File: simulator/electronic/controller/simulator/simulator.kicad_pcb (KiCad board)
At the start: 2 copper layers, 151 x 92.5 mm, 5 parts, among them J1 Mover1, J4 Mover2, J6 Rotator, J8 Mover3, U1 ESP32 D1 Mini

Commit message: design schematics
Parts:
- added D1: LED_PULSE, LED_SMD:LED_0805_2012Metric, B.Cu at (120.3, 75.2)
- added D10: LED_PULSE, LED_SMD:LED_0805_2012Metric, B.Cu at (49.5, 64.4)
- added D11: LED_DIR, LED_SMD:LED_RGB_5050-6, B.Cu at (47.6, 52.9)
- added D12: LED_SW, LED_SMD:LED_RGB_5050-6, B.Cu at (47.6, 59.6)
- added D2: LED_DIR, LED_SMD:LED_RGB_5050-6, B.Cu at (120.3, 80.1)
- added D3: LED_SW, LED_SMD:LED_RGB_5050-6, B.Cu at (120.3, 86.8)
- added D4: LED_PULSE, LED_SMD:LED_0805_2012Metric, B.Cu at (49.5, 84.1)
- added D5: LED_DIR, LED_SMD:LED_RGB_5050-6, B.Cu at (47.6, 72.6)
- added D6: LED_SW, LED_SMD:LED_RGB_5050-6, B.Cu at (47.6, 79.3)
- added D7: LED_PULSE, LED_SMD:LED_0805_2012Metric, B.Cu at (79.0, 64.4)
- added D8: LED_DIR, LED_SMD:LED_RGB_5050-6, B.Cu at (77.1, 52.9)
- added D9: LED_SW, LED_SMD:LED_RGB_5050-6, B.Cu at (77.1, 59.6)
- added J2: Conn_01x04_Socket, Connector_Extra:JST_XH_B4B-XH-A_1x04_P2.54mm_Vertical, F.Cu at (113.3, 91.4)
- added J3: Conn_01x04_Socket, Connector_Extra:JST_XH_B4B-XH-A_1x04_P2.54mm_Vertical, F.Cu at (113.3, 108.2)
- added J5: Conn_01x04_Socket, Connector_Extra:JST_XH_B4B-XH-A_1x04_P2.54mm_Vertical, F.Cu at (176.3, 84.8)
- added J7: Conn_01x04_Socket, Connector_Extra:JST_XH_B4B-XH-A_1x04_P2.54mm_Vertical, F.Cu at (176.3, 115.3)
- added R1: R_Small, Resistor_SMD:R_0805_2012Metric_Pad1.20x1.40mm_HandSolder, B.Cu at (127.0, 75.2)
- added R10: R_Small, Resistor_SMD:R_0805_2012Metric_Pad1.20x1.40mm_HandSolder, B.Cu at (68.6, 79.5)
- added R11: R_Small, Resistor_SMD:R_0805_2012Metric_Pad1.20x1.40mm_HandSolder, B.Cu at (68.6, 82.5)
- added R12: R_Small, Resistor_SMD:R_0805_2012Metric_Pad1.20x1.40mm_HandSolder, B.Cu at (68.6, 85.4)
- added R13: R_Small, Resistor_SMD:R_0805_2012Metric_Pad1.20x1.40mm_HandSolder, B.Cu at (98.1, 51.0)
- added R14: R_Small, Resistor_SMD:R_0805_2012Metric_Pad1.20x1.40mm_HandSolder, B.Cu at (98.1, 53.9)
- added R15: R_Small, Resistor_SMD:R_0805_2012Metric_Pad1.20x1.40mm_HandSolder, B.Cu at (98.1, 56.9)
- added R16: R_Small, Resistor_SMD:R_0805_2012Metric_Pad1.20x1.40mm_HandSolder, B.Cu at (98.1, 59.8)
- added R17: R_Small, Resistor_SMD:R_0805_2012Metric_Pad1.20x1.40mm_HandSolder, B.Cu at (98.1, 62.8)
- added R18: R_Small, Resistor_SMD:R_0805_2012Metric_Pad1.20x1.40mm_HandSolder, B.Cu at (98.1, 65.7)
- added R19: R_Small, Resistor_SMD:R_0805_2012Metric_Pad1.20x1.40mm_HandSolder, B.Cu at (68.6, 51.0)
- added R2: R_Small, Resistor_SMD:R_0805_2012Metric_Pad1.20x1.40mm_HandSolder, B.Cu at (127.0, 78.3)
- added R20: R_Small, Resistor_SMD:R_0805_2012Metric_Pad1.20x1.40mm_HandSolder, B.Cu at (68.6, 53.9)
- added R21: R_Small, Resistor_SMD:R_0805_2012Metric_Pad1.20x1.40mm_HandSolder, B.Cu at (68.6, 56.9)
- added R22: R_Small, Resistor_SMD:R_0805_2012Metric_Pad1.20x1.40mm_HandSolder, B.Cu at (68.6, 59.8)
- added R23: R_Small, Resistor_SMD:R_0805_2012Metric_Pad1.20x1.40mm_HandSolder, B.Cu at (68.6, 62.8)
- added R24: R_Small, Resistor_SMD:R_0805_2012Metric_Pad1.20x1.40mm_HandSolder, B.Cu at (68.6, 65.7)
- added R3: R_Small, Resistor_SMD:R_0805_2012Metric_Pad1.20x1.40mm_HandSolder, B.Cu at (127.0, 81.3)
- added R4: R_Small, Resistor_SMD:R_0805_2012Metric_Pad1.20x1.40mm_HandSolder, B.Cu at (68.6, 70.7)
- added R5: R_Small, Resistor_SMD:R_0805_2012Metric_Pad1.20x1.40mm_HandSolder, B.Cu at (127.0, 84.2)
- added R6: R_Small, Resistor_SMD:R_0805_2012Metric_Pad1.20x1.40mm_HandSolder, B.Cu at (127.0, 87.2)
- added R7: R_Small, Resistor_SMD:R_0805_2012Metric_Pad1.20x1.40mm_HandSolder, B.Cu at (127.0, 90.1)
- added R8: R_Small, Resistor_SMD:R_0805_2012Metric_Pad1.20x1.40mm_HandSolder, B.Cu at (68.6, 73.6)
- added R9: R_Small, Resistor_SMD:R_0805_2012Metric_Pad1.20x1.40mm_HandSolder, B.Cu at (68.6, 76.6)
- J1: value Mover1 -> Conn_01x04_Socket; footprint Connector_JST:JST_XH_B6B-XH-A_1x06_P2.50mm_Vertical -> Connector_Extra:JST_XH_B4B-XH-A_1x04_P2.54mm_Vertical
- J4: value Mover2 -> Conn_01x04_Socket; footprint Connector_JST:JST_XH_B6B-XH-A_1x06_P2.50mm_Vertical -> Connector_Extra:JST_XH_B4B-XH-A_1x04_P2.54mm_Vertical
- J6: value Rotator -> Conn_01x04_Socket; footprint Connector_JST:JST_XH_B6B-XH-A_1x06_P2.50mm_Vertical -> Connector_Extra:JST_XH_B4B-XH-A_1x04_P2.54mm_Vertical
- J8: value Mover3 -> Conn_01x04_Socket; footprint Connector_JST:JST_XH_B6B-XH-A_1x06_P2.50mm_Vertical -> Connector_Extra:JST_XH_B4B-XH-A_1x04_P2.54mm_Vertical
- moved J4 33.5 mm to (113.3, 122.4), turned to -90 degrees
- moved J8 13.3 mm to (176.3, 129.5)
- moved U1 12.2 mm to (145.5, 86.6)
- moved J1 11.8 mm to (113.3, 77.2), turned to -90 degrees
- moved J6 4.78 mm to (176.3, 98.8)
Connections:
- J1 pad 1: Net-(J1-Pin_1) -> /connection/PULSE
- J1 pad 2: Net-(J1-Pin_2) -> /connection/DIR
- J1 pad 3: GND -> /connection/ALARM
- J1 pad 4: unconnected-(J1-Pin_4-Pad4) -> GND
- J4 pad 1: Net-(J4-Pin_1) -> /connection1/SW_TOP
- J4 pad 2: Net-(J4-Pin_2) -> /connection1/SW_CENTER
- J4 pad 3: GND -> /connection1/SW_BOTTOM
- J4 pad 4: unconnected-(J4-Pin_4-Pad4) -> GND
- J6 pad 1: Net-(J6-Pin_1) -> /connection2/SW_TOP
- J6 pad 2: Net-(J6-Pin_2) -> /connection2/SW_CENTER
- J6 pad 3: GND -> /connection2/SW_BOTTOM
- J6 pad 4: unconnected-(J6-Pin_4-Pad4) -> GND
- J8 pad 1: Net-(J8-Pin_1) -> /connection3/SW_TOP
- J8 pad 2: Net-(J8-Pin_2) -> /connection3/SW_CENTER
- J8 pad 3: GND -> /connection3/SW_BOTTOM
- J8 pad 4: unconnected-(J8-Pin_4-Pad4) -> GND
- U1 pad 1: unconnected-(U1-GND-Pad1) -> GND
- U1 pad 10: Net-(J4-Pin_1) -> unconnected-(U1-IO_19/D6-Pad10)
- U1 pad 11: unconnected-(U1-IO_34-Pad11) -> /connection/SW_BOTTOM
- U1 pad 12: unconnected-(U1-IO_23/D7-Pad12) -> /connection1/DIR
- U1 pad 13: unconnected-(U1-IO_14/TMS-Pad13) -> /connection/DIR
- U1 pad 14: unconnected-(U1-IO_05/D8-Pad14) -> /connection1/PULSE
- U1 pad 16: unconnected-(U1-3V3-Pad16) -> 3V3
- U1 pad 17: Net-(J1-Pin_1) -> unconnected-(U1-IO_09/SD2-Pad17)
- U1 pad 20: Net-(J1-Pin_2) -> unconnected-(U1-IO_10/SD3-Pad20)
- U1 pad 22: unconnected-(U1-GND-Pad22) -> GND
- U1 pad 24: Net-(J6-Pin_2) -> /connection2/SW_BOTTOM
- U1 pad 25: unconnected-(U1-IO_22/D1/SCL-Pad25) -> /connection2/PULSE
- U1 pad 26: Net-(J8-Pin_2) -> /connection3/PULSE
- U1 pad 27: unconnected-(U1-IO_21/D2/SDA-Pad27) -> /connection2/DIR
- U1 pad 28: Net-(J4-Pin_2) -> /connection3/DIR
- U1 pad 29: unconnected-(U1-IO_17/D3-Pad29) -> /connection2/SW_TOP
- U1 pad 30: unconnected-(U1-IO_12/TDI-Pad30) -> /connection3/SW_TOP
- U1 pad 31: unconnected-(U1-IO_16/D4-Pad31) -> /connection2/SW_CENTER
- U1 pad 32: unconnected-(U1-IO_04-Pad32) -> /connection3/SW_CENTER
- U1 pad 33: unconnected-(U1-GND-Pad33) -> GND
- U1 pad 36: unconnected-(U1-IO_02-Pad36) -> /connection3/SW_BOTTOM
- U1 pad 4: unconnected-(U1-IO_36/SVP/A0-Pad4) -> /connection1/SW_BOTTOM
- U1 pad 5: unconnected-(U1-IO_39/SVN-Pad5) -> /connection/SW_TOP
- U1 pad 6: Net-(J6-Pin_1) -> /connection1/SW_CENTER
- U1 pad 7: unconnected-(U1-IO_35-Pad7) -> /connection/SW_CENTER
- U1 pad 8: unconnected-(U1-IO_18/D5-Pad8) -> /connection1/SW_TOP
- U1 pad 9: Net-(J8-Pin_1) -> /connection/PULSE
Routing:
- net Net-(J8-Pin_2): track 28.7 -> 0.00 mm
- net Net-(J6-Pin_2): track 19.1 -> 0.00 mm
- net unconnected-(D1-A-Pad2): track 0.00 -> 4.75 mm

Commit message: update simulator
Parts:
- added D10: LED_CENTER, LED_SMD:LED_0805_2012Metric, B.Cu at (200.1, 128.5)
- added D14: LED_TOP, LED_SMD:LED_0805_2012Metric, B.Cu at (219.5, 122.5)
- added D15: LED_UP, LED_SMD:LED_0805_2012Metric, B.Cu at (219.5, 125.5)
- added D16: LED_CENTER, LED_SMD:LED_0805_2012Metric, B.Cu at (219.5, 128.5)
- added D17: LED_BTM, LED_SMD:LED_0805_2012Metric, B.Cu at (219.5, 131.6)
- added D18: LED_DOWN, LED_SMD:LED_0805_2012Metric, B.Cu at (219.5, 134.6)
- added D20: LED_TOP, LED_SMD:LED_0805_2012Metric, B.Cu at (206.6, 122.5)
- added D21: LED_UP, LED_SMD:LED_0805_2012Metric, B.Cu at (206.6, 125.5)
- added D22: LED_CENTER, LED_SMD:LED_0805_2012Metric, B.Cu at (206.6, 128.5)
- added D23: LED_BTM, LED_SMD:LED_0805_2012Metric, B.Cu at (206.6, 131.6)
- added D24: LED_DOWN, LED_SMD:LED_0805_2012Metric, B.Cu at (206.6, 134.6)
- added D4: LED_CENTER, LED_SMD:LED_0805_2012Metric, B.Cu at (101.5, 90.9)
- D11, D5: value LED_DIR -> LED_BTM; footprint LED_SMD:LED_RGB_5050-6 -> LED_SMD:LED_0805_2012Metric
- D12, D6: value LED_SW -> LED_DOWN; footprint LED_SMD:LED_RGB_5050-6 -> LED_SMD:LED_0805_2012Metric
- D2, D8: value LED_DIR -> LED_TOP; footprint LED_SMD:LED_RGB_5050-6 -> LED_SMD:LED_0805_2012Metric
- D3, D9: value LED_SW -> LED_UP; footprint LED_SMD:LED_RGB_5050-6 -> LED_SMD:LED_0805_2012Metric
- moved D11 171.7 mm to (200.1, 131.6)
- moved D12 170.0 mm to (200.1, 134.6)
- moved D8 141.3 mm to (200.1, 122.5)
- moved D9 139.6 mm to (200.1, 125.5)
- moved D5 58.0 mm to (101.5, 94.0)
- moved D6 56.8 mm to (101.5, 97.0)
- moved D2 19.3 mm to (101.5, 84.8)
- moved D3 18.8 mm to (101.5, 87.9)
- turned R2 to 0 degrees
- turned R3 to 0 degrees
- turned R4 to 0 degrees
- turned R5 to 0 degrees
- turned R6 to 0 degrees
- renumbered D7 to D13, D10 to D19, D4 to D7, R11 to R10, R12 to R11, R10 to R12, R15 to R14, R14 to R15, R17 to R16, R18 to R17, R16 to R18, R7 to R2, R21 to R20, R20 to R21, R23 to R22, R24 to R23, R22 to R24, R2 to R3, R6 to R4, R3 to R6, R4 to R7, R9 to R8, R8 to R9
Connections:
- D1 pad 2: unconnected-(D1-A-Pad2) -> Net-(D1-A)
- D11 pad 1: unconnected-(D11-RK-Pad1) -> Net-(D11-K)
- D12 pad 1: 3V3 -> Net-(D12-K)
- D2 pad 1: unconnected-(D2-RK-Pad1) -> Net-(D2-K)
- D3 pad 1: 3V3 -> GND
- D3 pad 2: 3V3 -> Net-(D3-A)
- D5 pad 1: unconnected-(D5-RK-Pad1) -> Net-(D5-K)
- D6 pad 1: 3V3 -> Net-(D6-K)
- D8 pad 1: unconnected-(D8-RK-Pad1) -> Net-(D8-K)
- D9 pad 1: 3V3 -> GND
- D9 pad 2: 3V3 -> Net-(D9-A)
- R1 pad 1: unconnected-(D1-A-Pad2) -> Net-(D1-A)
- R10 pad 1: Net-(D6-GA) -> Net-(D10-K)
- R11 pad 1: Net-(D6-BA) -> Net-(D11-K)
- R12 pad 1: Net-(D5-GA) -> Net-(D12-K)
- R14 pad 1: Net-(D9-RA) -> Net-(D14-K)
- R15 pad 1: Net-(D8-BA) -> Net-(D15-A)
- R16 pad 1: Net-(D9-GA) -> Net-(D16-K)
- R17 pad 1: Net-(D9-BA) -> Net-(D17-K)
- R18 pad 1: Net-(D8-GA) -> Net-(D18-K)
- R2 pad 1: Net-(D3-RA) -> Net-(D2-K)
- R20 pad 1: Net-(D12-RA) -> Net-(D20-K)
- R21 pad 1: Net-(D11-BA) -> Net-(D21-A)
- R22 pad 1: Net-(D12-GA) -> Net-(D22-K)
- R23 pad 1: Net-(D12-BA) -> Net-(D23-K)
- R24 pad 1: Net-(D11-GA) -> Net-(D24-K)
- R3 pad 1: Net-(D2-BA) -> Net-(D3-A)
- R4 pad 1: Net-(D3-GA) -> Net-(D4-K)
- R5 pad 1: Net-(D3-BA) -> Net-(D5-K)
- R6 pad 1: Net-(D2-GA) -> Net-(D6-K)
- R8 pad 1: Net-(D6-RA) -> Net-(D8-K)
- R9 pad 1: Net-(D5-BA) -> Net-(D9-A)
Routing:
- net /connection/PULSE: track 0.00 -> 11.6 mm
- net unconnected-(D1-A-Pad2): track 4.75 -> 0.00 mm
- net Net-(D1-A): track 0.00 -> 4.75 mm

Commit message: update simulator
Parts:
- moved D19 128.4 mm to (177.3, 77.2)
- moved D13 113.6 mm to (177.3, 121.4)
- moved R22 109.9 mm to (172.7, 91.9)
- moved R23 108.9 mm to (172.7, 94.5)
- moved R24 108.8 mm to (172.7, 97.0)
- moved R19 107.4 mm to (172.7, 77.2)
- moved R20 107.3 mm to (172.7, 79.8)
- moved R21 106.5 mm to (172.7, 82.3)
- moved R13 102.6 mm to (172.7, 121.4)
- moved R14 102.3 mm to (172.7, 124.0)
- moved R15 100.0 mm to (172.7, 126.5)
- moved R16 89.7 mm to (172.7, 106.7)
- moved D9 88.8 mm to (114.3, 111.8)
- moved R17 87.9 mm to (172.7, 109.2)
- moved R18 87.7 mm to (172.7, 111.8)
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- renumbered D8 to D10, D10 to D11, D11 to D12, D15 to D14, D18 to D15, D14 to D16, D16 to D17, D17 to D18, D3 to D2, D21 to D20, D24 to D21, D20 to D22, D22 to D23, D23 to D24, D6 to D3, D2 to D4, D4 to D5, D5 to D6, D9 to D8, D12 to D9, R8 to R10, R10 to R11, R11 to R12, R15 to R14, R18 to R15, R14 to R16, R16 to R17, R17 to R18, R3 to R2, R21 to R20, R24 to R21, R20 to R22, R22 to R23, R23 to R24, R6 to R3, R2 to R4, R4 to R5, R5 to R6, R9 to R8, R12 to R9
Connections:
- U1 pad 24: /connection2/SW_BOTTOM -> /connection2/DIR
- U1 pad 27: /connection2/DIR -> /connection2/SW_BOTTOM
- U1 pad 29: /connection2/SW_TOP -> /connection2/SW_CENTER
- U1 pad 31: /connection2/SW_CENTER -> /connection2/SW_TOP
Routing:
- net /connection1/SW_BOTTOM: track 0.00 -> 63.3 mm
- net /connection1/SW_CENTER: track 0.00 -> 58.0 mm
- net /connection2/PULSE: track 0.00 -> 54.6 mm
- net /connection1/SW_TOP: track 0.00 -> 51.3 mm
- net 3V3: track 0.00 -> 49.3 mm
- net /connection2/SW_BOTTOM: track 0.00 -> 43.7 mm
- net /connection1/DIR: track 0.00 -> 42.5 mm
- net /connection2/SW_CENTER: track 0.00 -> 38.4 mm
- net /connection1/PULSE: track 0.00 -> 35.4 mm
- net /connection2/SW_TOP: track 0.00 -> 33.2 mm
- net /connection/DIR: track 0.00 -> 16.4 mm
- net /connection3/DIR: track 0.00 -> 16.0 mm
- net /connection3/SW_TOP: track 0.00 -> 14.9 mm
- net /connection3/SW_CENTER: track 0.00 -> 14.9 mm
- net /connection/SW_BOTTOM: track 0.00 -> 14.5 mm
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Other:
- board size 151 x 92.5 mm -> 76.3 x 69.6 mm

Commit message: update simulator
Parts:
- J1, J3, J5, J7: value Conn_01x04_Socket -> Conn_01x03_Socket; footprint Connector_Extra:JST_XH_B4B-XH-A_1x04_P2.54mm_Vertical -> Connector_JST:JST_XH_B3B-XH-A_1x03_P2.50mm_Vertical
- moved D14 3.05 mm to (177.3, 127.0)
- moved R14 3.05 mm to (172.7, 127.0)
- moved D13 3.05 mm to (177.3, 124.5)
- moved D15 3.05 mm to (177.3, 129.5)
- moved R13 3.05 mm to (172.7, 124.5)
- moved R15 3.05 mm to (172.7, 129.5)
- moved D1 2.54 mm to (113.8, 94.5)
- moved D2 2.54 mm to (113.8, 97.0)
- moved D3 2.54 mm to (113.9, 99.5)
- moved R1 2.54 mm to (118.4, 94.5)
- moved R2 2.54 mm to (118.4, 97.0)
- moved R3 2.54 mm to (118.4, 99.6)
- moved J5 0.59 mm to (169.2, 122.0)
- moved J7 0.08 mm to (169.2, 77.3)
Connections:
- D1 pad 1: GND -> Net-(D1-K)
- D13 pad 1: GND -> Net-(D13-K)
- D14 pad 1: GND -> Net-(D13-K)
- D19 pad 1: GND -> Net-(D19-K)
- D2 pad 1: GND -> Net-(D1-K)
- D20 pad 1: GND -> Net-(D19-K)
- D7 pad 1: GND -> Net-(D7-K)
- D8 pad 1: GND -> Net-(D7-K)
- J1 pad 1: /connection/PULSE -> GND
- J1 pad 2: /connection/DIR -> /connection/PULSE
- J1 pad 3: /connection/ALARM -> /connection/DIR
- J2 pad 4: GND -> Net-(D1-K)
- J3 pad 1: /connection1/PULSE -> GND
- J3 pad 2: /connection1/DIR -> /connection1/PULSE
- J3 pad 3: /connection1/ALARM -> /connection1/DIR
- J4 pad 4: GND -> Net-(D7-K)
- J5 pad 1: /connection2/PULSE -> GND
- J5 pad 2: /connection2/DIR -> /connection2/PULSE
- J5 pad 3: /connection2/ALARM -> /connection2/DIR
- J6 pad 4: GND -> Net-(D13-K)
- J7 pad 1: /connection3/PULSE -> GND
- J7 pad 2: /connection3/DIR -> /connection3/PULSE
- J7 pad 3: /connection3/ALARM -> /connection3/DIR
- J8 pad 4: GND -> Net-(D19-K)
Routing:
- net /connection2/PULSE: track 54.6 -> 58.6 mm
- net GND: track 7.65 -> 10.5 mm
- net Net-(D7-K): track 0.00 -> 2.57 mm
- net Net-(D19-K): track 0.00 -> 2.54 mm
- net Net-(D13-K): track 0.00 -> 2.54 mm
- net /connection/DIR: track 16.4 -> 17.6 mm
- net /connection3/DIR: track 16.0 -> 15.0 mm

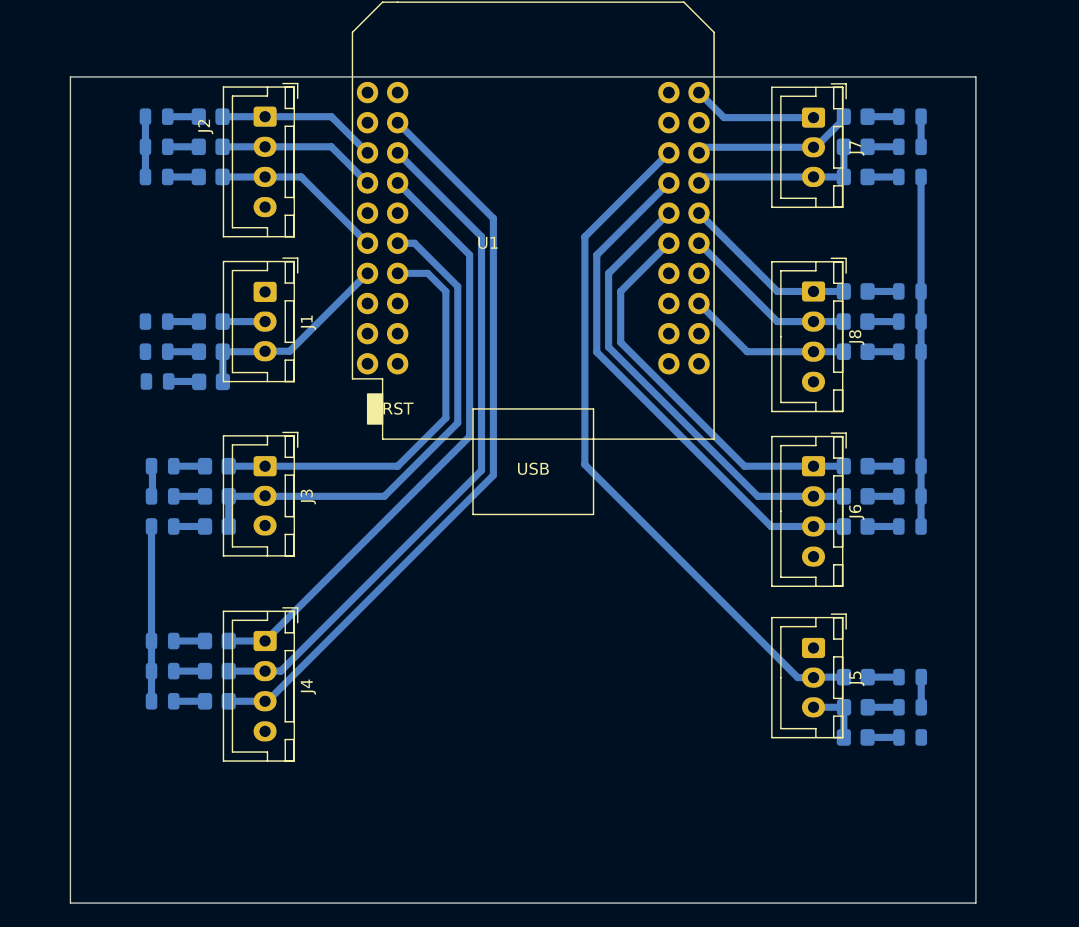
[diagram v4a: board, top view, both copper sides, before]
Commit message: shaped schematic and PCB added printed documentation of PCB
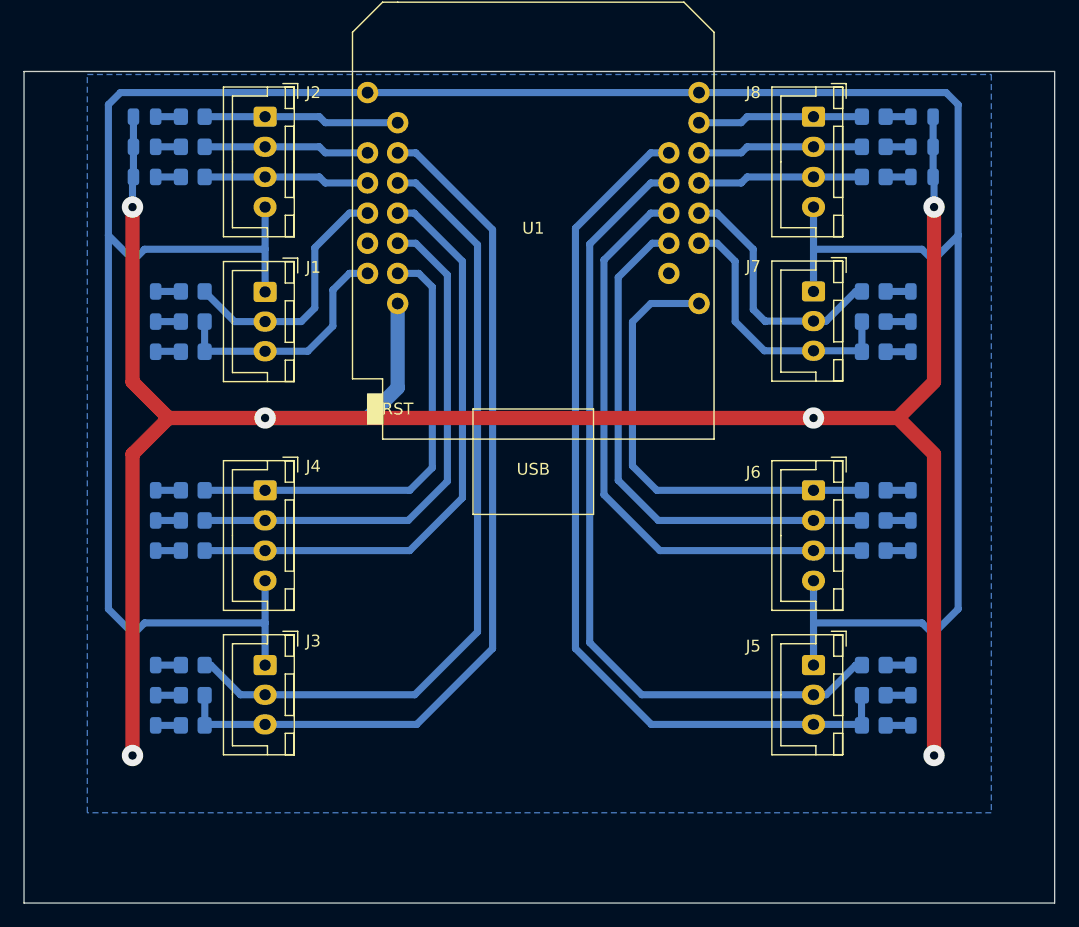
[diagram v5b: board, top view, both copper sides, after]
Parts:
- R1, R10, R11, R12, R13, R14, R15, R16, R17, R18, R19, R2, R20, R21, R22, R23, R24, R3, R4, R5, R6, R7, R8, R9: value R_Small -> 150R
- moved R7 16.9 mm to (116.8, 123.4)
- moved R8 16.9 mm to (116.8, 126.0)
- moved R9 16.9 mm to (116.8, 128.5)
- moved D7 16.8 mm to (112.8, 123.4)
- moved D8 16.8 mm to (112.8, 126.0)
- moved D9 16.8 mm to (112.8, 128.5)
- moved J3 16.8 mm to (122.9, 123.4)
- moved R23 14.8 mm to (174.2, 79.8)
- moved R19 14.8 mm to (174.2, 91.9)
- moved R20 14.8 mm to (174.2, 94.5)
- moved R21 14.8 mm to (174.2, 97.0)
- moved R22 14.8 mm to (174.2, 77.2)
- moved R24 14.8 mm to (174.2, 82.3)
- moved D19 14.8 mm to (178.3, 91.9)
- moved D20 14.8 mm to (178.3, 94.5)
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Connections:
- net /connection/DIR renamed M1_DIR
- net /connection/PULSE renamed M1_PULSE
- D1 pad 1: Net-(D1-K) -> GND
- D13 pad 1: Net-(D13-K) -> GND
- D14 pad 1: Net-(D13-K) -> GND
- D19 pad 1: Net-(D19-K) -> GND
- D2 pad 1: Net-(D1-K) -> GND
- D20 pad 1: Net-(D19-K) -> GND
- D7 pad 1: Net-(D7-K) -> GND
- D8 pad 1: Net-(D7-K) -> GND
- J2 pad 1: /connection/SW_TOP -> M1_SW_TOP
- J2 pad 2: /connection/SW_CENTER -> M1_SW_CTR
- J2 pad 3: /connection/SW_BOTTOM -> M1_SW_BTM
- J2 pad 4: Net-(D1-K) -> GND
- J3 pad 2: /connection1/PULSE -> M2_PULSE
- J3 pad 3: /connection1/DIR -> M2_DIR
- J4 pad 1: /connection1/SW_TOP -> M2_SW_TOP
- J4 pad 2: /connection1/SW_CENTER -> M2_SW_CTR
- J4 pad 3: /connection1/SW_BOTTOM -> M2_SW_BTM
- J4 pad 4: Net-(D7-K) -> GND
- J5 pad 2: /connection2/PULSE -> M3_PULSE
- J5 pad 3: /connection2/DIR -> M3_DIR
- J6 pad 1: /connection2/SW_TOP -> M3_SW_TOP
- J6 pad 2: /connection2/SW_CENTER -> M3_SW_CTR
- J6 pad 3: /connection2/SW_BOTTOM -> M3_SW_BTM
- J6 pad 4: Net-(D13-K) -> GND
- J7 pad 2: /connection3/PULSE -> M4_PULSE
- J7 pad 3: /connection3/DIR -> M4_DIR
- J8 pad 1: /connection3/SW_TOP -> M4_SW_LEFT
- J8 pad 2: /connection3/SW_CENTER -> M4_SW_CTR
- J8 pad 3: /connection3/SW_BOTTOM -> M4_SW_RIGHT
- J8 pad 4: Net-(D19-K) -> GND
- R10 pad 2: /connection1/SW_TOP -> M2_SW_TOP
- R11 pad 2: /connection1/SW_CENTER -> M2_SW_CTR
- R12 pad 2: /connection1/SW_BOTTOM -> M2_SW_BTM
- R13 pad 2: /connection2/PULSE -> M3_PULSE
- R14 pad 2: /connection2/DIR -> M3_DIR
- R15 pad 2: /connection2/DIR -> M3_DIR
- R16 pad 2: /connection2/SW_TOP -> M3_SW_TOP
- R17 pad 2: /connection2/SW_CENTER -> M3_SW_CTR
- R18 pad 2: /connection2/SW_BOTTOM -> M3_SW_BTM
- R19 pad 2: /connection3/PULSE -> M4_PULSE
- R20 pad 2: /connection3/DIR -> M4_DIR
- R21 pad 2: /connection3/DIR -> M4_DIR
- R22 pad 2: /connection3/SW_TOP -> M4_SW_LEFT
- R23 pad 2: /connection3/SW_CENTER -> M4_SW_CTR
- R24 pad 2: /connection3/SW_BOTTOM -> M4_SW_RIGHT
- R4 pad 2: /connection/SW_TOP -> M1_SW_TOP
- R5 pad 2: /connection/SW_CENTER -> M1_SW_CTR
- R6 pad 2: /connection/SW_BOTTOM -> M1_SW_BTM
- R7 pad 2: /connection1/PULSE -> M2_PULSE
- R8 pad 2: /connection1/DIR -> M2_DIR
- R9 pad 2: /connection1/DIR -> M2_DIR
- U1 pad 10: unconnected-(U1-IO_19/D6-Pad10) -> M2_SW_BTM
- U1 pad 11: /connection/SW_BOTTOM -> unconnected-(U1-IO_34-Pad11)
- U1 pad 12: /connection1/DIR -> M2_SW_CTR
- U1 pad 14: /connection1/PULSE -> M2_SW_TOP
- U1 pad 24: /connection2/DIR -> M4_SW_LEFT
- U1 pad 25: /connection2/PULSE -> M3_DIR
- U1 pad 26: /connection3/PULSE -> M4_SW_CTR
- U1 pad 27: /connection2/SW_BOTTOM -> M3_PULSE
- U1 pad 28: /connection3/DIR -> M4_SW_RIGHT
- U1 pad 29: /connection2/SW_CENTER -> M3_SW_BTM
- U1 pad 30: /connection3/SW_TOP -> M4_PULSE
- U1 pad 31: /connection2/SW_TOP -> M3_SW_CTR
- U1 pad 32: /connection3/SW_CENTER -> M4_DIR
- U1 pad 33: GND -> unconnected-(U1-GND-Pad33)
- U1 pad 36: /connection3/SW_BOTTOM -> M3_SW_TOP
- U1 pad 4: /connection1/SW_BOTTOM -> M1_SW_TOP
- U1 pad 5: /connection/SW_TOP -> M1_SW_CTR
- U1 pad 6: /connection1/SW_CENTER -> M2_DIR
- U1 pad 7: /connection/SW_CENTER -> M1_SW_BTM
- U1 pad 8: /connection1/SW_TOP -> M2_PULSE
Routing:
- net GND: track 10.5 -> 262.5 mm
- net 3V3: track 49.3 -> 252.0 mm, vias 0 -> 6
- net M2_DIR: track 0.00 -> 75.4 mm
- net M3_DIR: track 0.00 -> 75.2 mm
- net M3_PULSE: track 0.00 -> 68.2 mm
- net M2_PULSE: track 0.00 -> 67.8 mm
- net /connection1/SW_BOTTOM: track 63.3 -> 0.00 mm
- net /connection2/PULSE: track 58.6 -> 0.00 mm
- net /connection1/SW_CENTER: track 58.0 -> 0.00 mm
- net /connection1/SW_TOP: track 51.3 -> 0.00 mm
- net M2_SW_BTM: track 0.00 -> 50.6 mm
- net M3_SW_BTM: track 0.00 -> 50.6 mm
- net M2_SW_CTR: track 0.00 -> 44.5 mm
- net M3_SW_CTR: track 0.00 -> 44.5 mm
- net /connection2/SW_BOTTOM: track 43.7 -> 0.00 mm
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- added copper zone on B.Cu, net GND
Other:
- board size 76.3 x 69.6 mm -> 86.9 x 70.1 mm
